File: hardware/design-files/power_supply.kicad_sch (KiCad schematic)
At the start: 8 parts, among them J1 230VAC_IN, U1 HLK-PM01, U2 AMS1117-3.3

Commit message: feat(hardware): update KiCad schematics with component symbols and layout refinements
- Add ADS1115 16-bit I2C ADC symbol to CT sensor schematic
- Add AudioJack2 connector symbol for analog signal input
- Update ESP32 module schematic with refined pin configurations
- Update power supply schematic with improved component placement
- Update relay driver schematic with optimized routing
- Refine PCB layout in gateway.kicad_pcb with better trace routing
- Update project settings in gateway.kicad_pro for design rule compliance
- Add project rules configuration in gateway.kicad_prl for manufacturing constraints
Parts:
- removed C1: 100uF/16V, Capacitor_THT:CP_Radial_D6.3mm_P2.50mm, symbol Device:C_Polarized
- removed C2: 10uF, Capacitor_SMD:C_0805_2012Metric, symbol Device:C
- removed C3: 22uF, Capacitor_SMD:C_0805_2012Metric, symbol Device:C
- removed D1: P6KE250CA, Diode_THT:D_DO-201_P15.24mm_Horizontal, symbol Device:D_TVS_bidirectional
- removed F1: 5A Fast-Blow, Fuse:Fuseholder5x20_Horiz_SemiClosed_Casing10x25mm, symbol Device:Fuse
- removed J1: 230VAC_IN, TerminalBlock:TerminalBlock_bornier-2_P5.08mm, symbol Connector:Screw_Terminal_01x02
- removed U1: HLK-PM01, Converter_ACDC:Converter_ACDC_HiLink_HLK-PMxx, symbol Converter_ACDC:HLK-PM01
- removed U2: AMS1117-3.3, Package_TO_SOT_SMD:SOT-223-3_TabPin2, symbol Regulator_Linear:AMS1117-3.3
- added J1: Conn_01x02, Connector_PinHeader_2.54mm:PinHeader_1x02_P2.54mm_Vertical, symbol Connector_Generic:Conn_01x02
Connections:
- net GND: now also J1.2 (Pin_2)
- new net +5V: J1.1 (Pin_1)

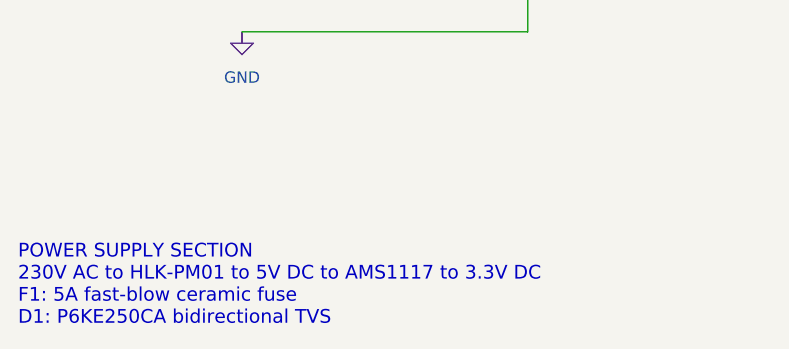
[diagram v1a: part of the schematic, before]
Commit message: feat(hardware): update PCB layout and component footprints
- Reposition ADS1115 ADC module on PCB (moved from 84.35,28 to 60.5,49.35 with 180° rotation)
- Update CT sensor connector footprint from PinHeader to 3.5mm audio jack (Switronic ST-005-G)
- Correct ESP32 module connector footprint from 1x02 to 1x06 pin header
- Regenerate component UUIDs and silk screen coordinates to reflect new placements
- Optimize PCB layout for improved signal routing and component accessibility
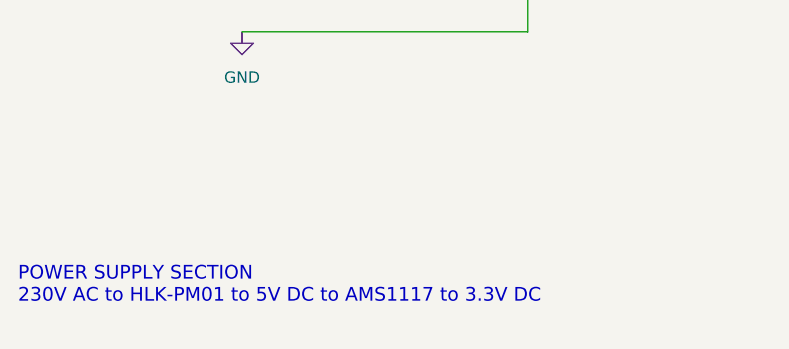
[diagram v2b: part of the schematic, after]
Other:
- note added: "POWER SUPPLY SECTION 230V AC to HLK-PM01 to 5V DC to AMS1117 to 3.3V DC"
- note removed: "POWER SUPPLY SECTION 230V AC to HLK-PM01 to 5V DC to AMS1117 to 3.3V DC F1: 5A fast-blow ceramic fuse D1: P6KE250CA bidirectional TVS"
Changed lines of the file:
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@@
 		(company "Ailsh Giri")
 		(comment 1 "Hi-Link HLK-PM01 (230VAC to 5VDC) + AMS1117-3.3")
-		(comment 2 "Fused AC input with 5A fast-blow ceramic fuse")
+		(comment 2 "AC/DC power conversion for ESP32 and relay module")
 	)
-	(text "POWER SUPPLY SECTION\n230V AC to HLK-PM01 to 5V DC to AMS1117 to 3.3V DC\nF1: 5A fast-blow ceramic fuse\nD1: P6KE250CA bidirectional TVS"
+	(text "POWER SUPPLY SECTION\n230V AC to HLK-PM01 to 5V DC to AMS1117 to 3.3V DC"
 		(exclude_from_sim no)
 		(at 25.908 100.584 0)
